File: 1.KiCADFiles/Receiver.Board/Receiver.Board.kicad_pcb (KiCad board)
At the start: 4 copper layers, 177 x 152 mm, 204 parts, among them J5 Conn_Coaxial_Out

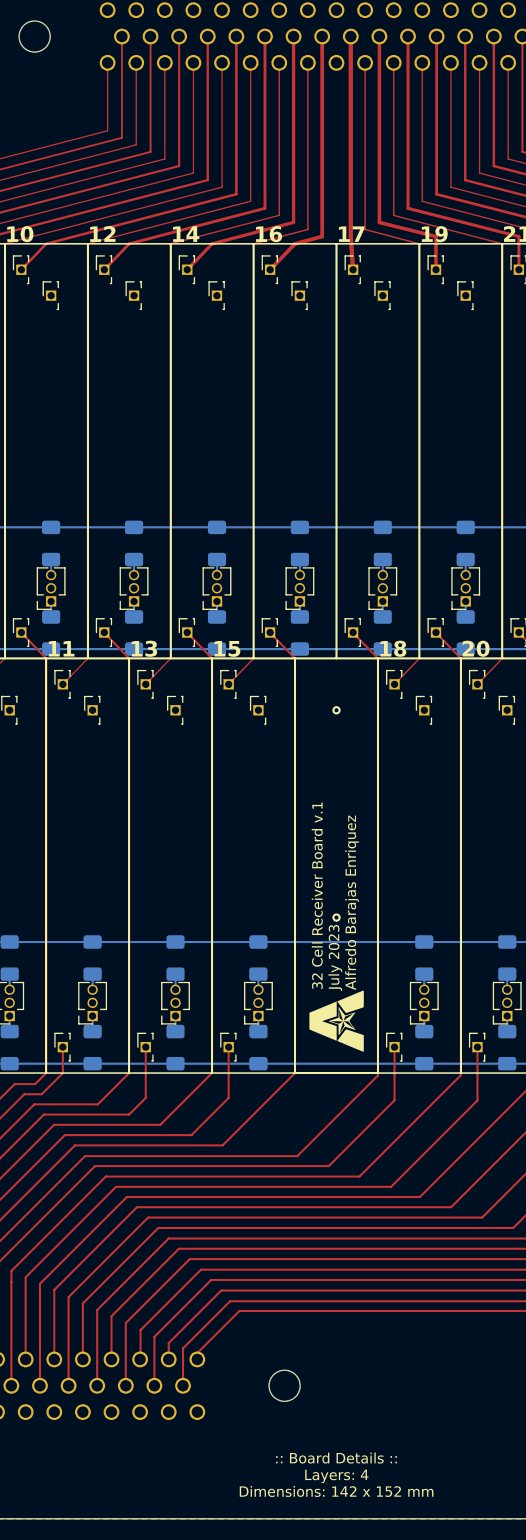
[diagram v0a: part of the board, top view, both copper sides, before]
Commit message: Minor Fixes, Updated Excel Sheet to contain approx surface area
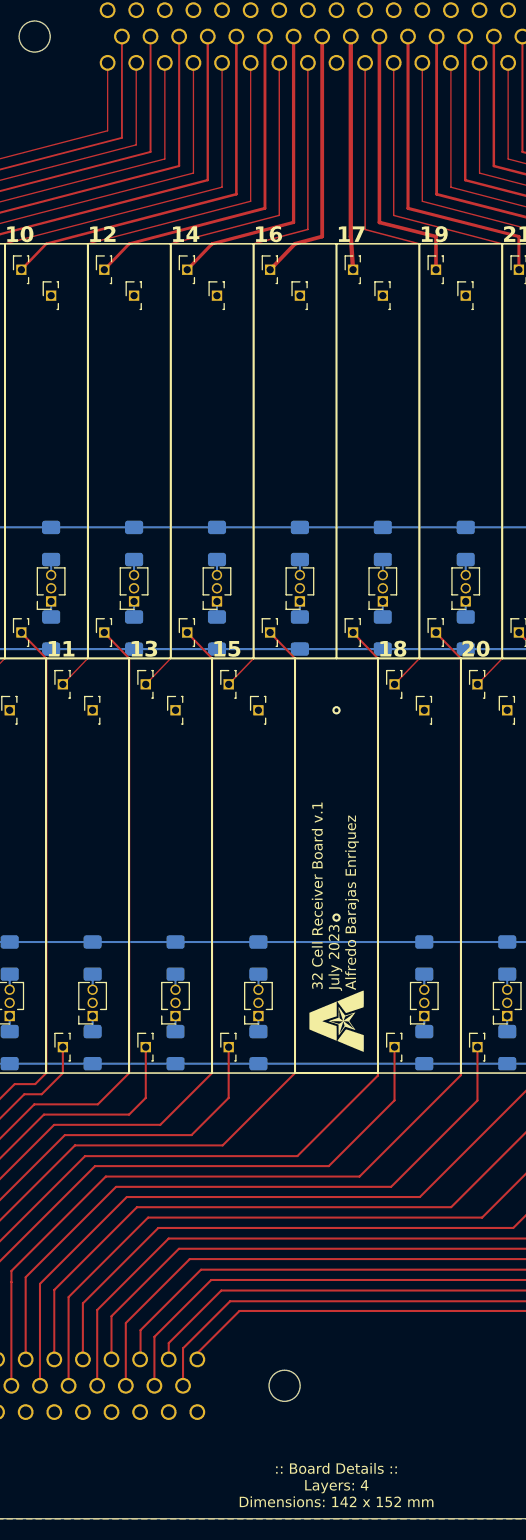
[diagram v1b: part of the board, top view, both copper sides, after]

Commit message: Minor Graphic Changes
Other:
- board text added: ":: Board Details :: Layers: 4 Dimensions: 32 x 62 mm"
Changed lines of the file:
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@@
     (stroke (width 0.2) (type default)) (layer "F.Cu"))
   (gr_line (start 173.6 122.5) (end 176 120)
-    (stroke (width 0.127736) (type default)) (layer "F.Cu"))
+    (stroke (width 0.127734) (type default)) (layer "F.Cu"))
   (gr_line (start 213.6 122.5) (end 216 120)
     (stroke (width 0.135235) (type default)) (layer "F.Cu"))
@@
     (stroke (width 0.248012) (type default)) (layer "F.Cu"))
   (gr_line (start 176 80) (end 176 120)
-    (stroke (width 0.127736) (type default)) (layer "F.Cu"))
+    (stroke (width 0.127734) (type default)) (layer "F.Cu"))
   (gr_line (start 149.6 122.5) (end 152 120)
     (stroke (width 0.109512) (type default)) (layer "F.Cu"))
@@
     (stroke (width 0.121019) (type default)) (layer "F.Cu"))
   (gr_line (start 176 80) (end 191.72 75.893)
-    (stroke (width 0.127736) (type default)) (layer "F.Cu"))
+    (stroke (width 0.127734) (type default)) (layer "F.Cu"))
   (gr_line (start 245.6 122.5) (end 248 120)
     (stroke (width 0.114979) (type default)) (layer "F.Cu"))
@@
     (stroke (width 0.187441) (type default)) (layer "F.Cu"))
   (gr_line (start 191.72 62.54) (end 191.72 75.893)
-    (stroke (width 0.127736) (type default)) (layer "F.Cu"))
+    (stroke (width 0.127734) (type default)) (layer "F.Cu"))
   (gr_line (start 240 80) (end 240 120)
     (stroke (width 0.115647) (type default)) (layer "F.Cu"))
@@
   (gr_line (start 133.6 153.5) (end 133.6 157.5)
     (stroke (width 0.15) (type default)) (layer "User.8"))
+  (gr_text ":: Board Details ::\nLayers: 4\nDimensions: 32 x 62 mm" (at 106.374 113.789) (layer "B.SilkS")
+    (effects (font (size 1 1) (thickness 0.15)) (justify bottom mirror))
+  )
+  (gr_text ":: Board Details ::\nLayers: 4\nDimensions: 142 x 152 mm" (at 200 202) (layer "B.SilkS")
+    (effects (font (size 1 1) (thickness 0.15)) (justify bottom mirror))
+  )
   (gr_text "13" (at 180 120) (layer "F.SilkS")
     (effects (font (size 1.5 1.5) (thickness 0.3) bold) (justify left bottom))
@@
     (effects (font (size 1 1) (thickness 0.15)) (justify left bottom))
   )
-  (gr_text ":: Board Details ::\nLayers: 4\nDimensions: 142 x 152 mm" (at 200 202) (layer "F.SilkS")
-    (effects (font (size 1 1) (thickness 0.15)) (justify bottom))
-  )
   (gr_text "4" (at 144 80) (layer "F.SilkS")
     (effects (font (size 1.5 1.5) (thickness 0.3) bold) (justify left bottom))
@@
         (xy 173.301458 60.621725)
         (xy 173.360287 60.313333)
-        (xy 173.38 60)
       )
     )

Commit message: Added Repository Link to Receiver Board
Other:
- board text added: ":: Board Details :: Layers: 4 Dimensions: 142 x 152 mm :: More Info :: https://github.com/barajasalfredo13/32.Channel.Amp"
- board text removed: ":: Board Details :: Layers: 4 Dimensions: 142 x 152 mm"
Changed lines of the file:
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@@
     (stroke (width 0.2) (type default)) (layer "F.Cu"))
   (gr_line (start 173.6 122.5) (end 176 120)
-    (stroke (width 0.127734) (type default)) (layer "F.Cu"))
+    (stroke (width 0.127733) (type default)) (layer "F.Cu"))
   (gr_line (start 213.6 122.5) (end 216 120)
     (stroke (width 0.135235) (type default)) (layer "F.Cu"))
@@
     (stroke (width 0.248012) (type default)) (layer "F.Cu"))
   (gr_line (start 176 80) (end 176 120)
-    (stroke (width 0.127734) (type default)) (layer "F.Cu"))
+    (stroke (width 0.127733) (type default)) (layer "F.Cu"))
   (gr_line (start 149.6 122.5) (end 152 120)
     (stroke (width 0.109512) (type default)) (layer "F.Cu"))
@@
     (stroke (width 0.121019) (type default)) (layer "F.Cu"))
   (gr_line (start 176 80) (end 191.72 75.893)
-    (stroke (width 0.127734) (type default)) (layer "F.Cu"))
+    (stroke (width 0.127733) (type default)) (layer "F.Cu"))
   (gr_line (start 245.6 122.5) (end 248 120)
     (stroke (width 0.114979) (type default)) (layer "F.Cu"))
@@
     (stroke (width 0.187441) (type default)) (layer "F.Cu"))
   (gr_line (start 191.72 62.54) (end 191.72 75.893)
-    (stroke (width 0.127734) (type default)) (layer "F.Cu"))
+    (stroke (width 0.127733) (type default)) (layer "F.Cu"))
   (gr_line (start 240 80) (end 240 120)
     (stroke (width 0.115647) (type default)) (layer "F.Cu"))
@@
     (effects (font (size 1 1) (thickness 0.15)) (justify bottom mirror))
   )
-  (gr_text ":: Board Details ::\nLayers: 4\nDimensions: 142 x 152 mm" (at 200 202) (layer "B.SilkS")
+  (gr_text ":: Board Details ::\nLayers: 4\nDimensions: 142 x 152 mm\n:: More Info ::\nhttps://github.com/barajasalfredo13/32.Channel.Amp" (at 200 202) (layer "B.SilkS")
     (effects (font (size 1 1) (thickness 0.15)) (justify bottom mirror))
   )
